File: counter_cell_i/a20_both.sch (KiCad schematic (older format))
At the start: 30 parts, among them U20001 74HC02, U20002 74HC04, U20003 74HC02, U20004 74HC02, U20005 74HC27, U20006 74HC02, U20007 74HC02, U20008 74HC27, U20009 74HC27, U20010 74HC02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

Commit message: Initial conditions for the counter cells
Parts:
- U20003, U20006, U20016, U20019: Initial (none) -> 1

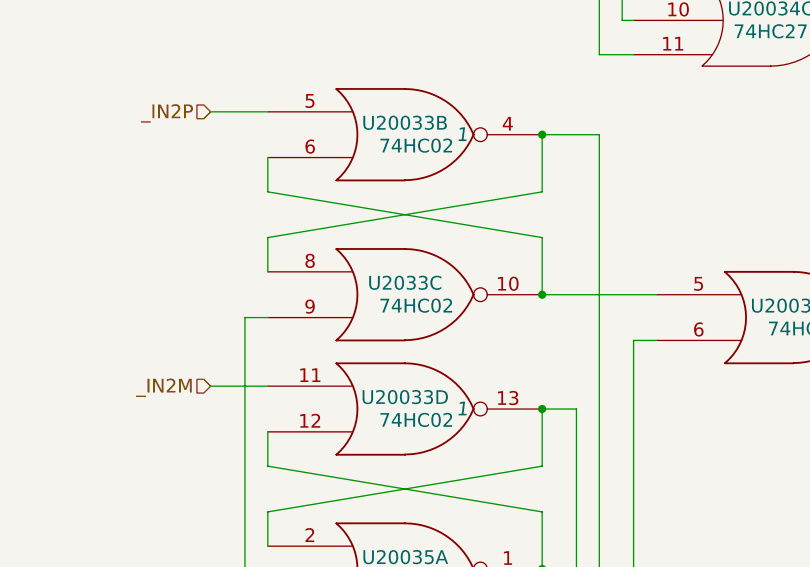
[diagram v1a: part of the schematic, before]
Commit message: Corrected some bad identifiers found by Quartus
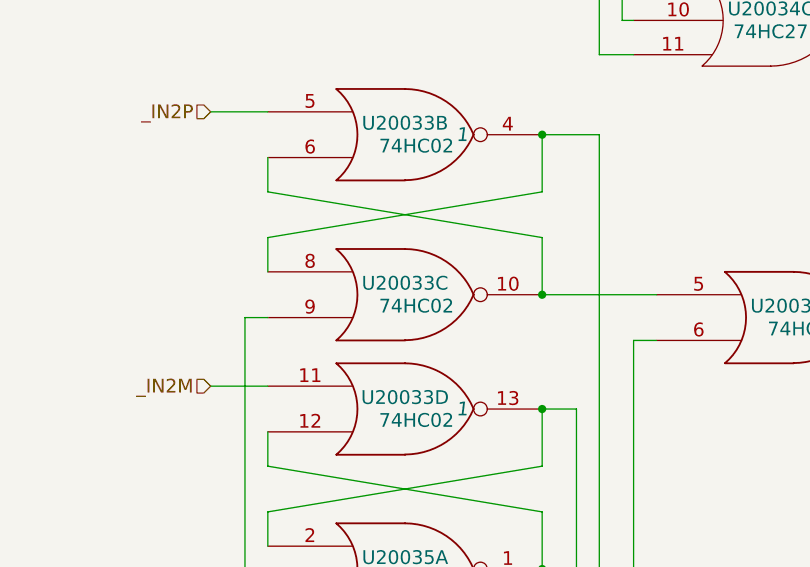
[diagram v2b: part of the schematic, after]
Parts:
- renumbered U2004 to U20004
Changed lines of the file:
@@
 _IN2P
 $Comp
-L 74HC02 U2004
+L 74HC02 U20004
 U 3 1 56E54AEA
 P 4400 5150
-AR Path="/56E4FF16/56E54AEA" Ref="U2004"  Part="3"
-AR Path="/56EE947A/56E54AEA" Ref="U2033"  Part="3"
-F 0 "U2033" H 4400 5200 60  0000 C CNN
+AR Path="/56E4FF16/56E54AEA" Ref="U20004"  Part="3"
+AR Path="/56EE947A/56E54AEA" Ref="U20033"  Part="3"
+F 0 "U20033" H 4400 5200 60  0000 C CNN
 F 1 "74HC02" H 4450 5100 60  0000 C CNN
 F 2 "" H 4400 5150 60  0000 C CNN

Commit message: Fixed not->1-input nor in the rest of the modules.
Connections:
- wire segments 438 -> 460
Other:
- moved on the sheet: U20001A, U20001B, U20001C, U20001D, U20002A, U20002B, U20002C, U20002D, U20002E, U20002F, U20003A, U20003B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
